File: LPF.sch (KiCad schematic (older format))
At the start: 142 parts, among them J1 Conn_02x05_Counter_Clockwise, P1 SMA, P2 SMA, P3 SMA, P4 SMA, P5 SMA, P6 SMA

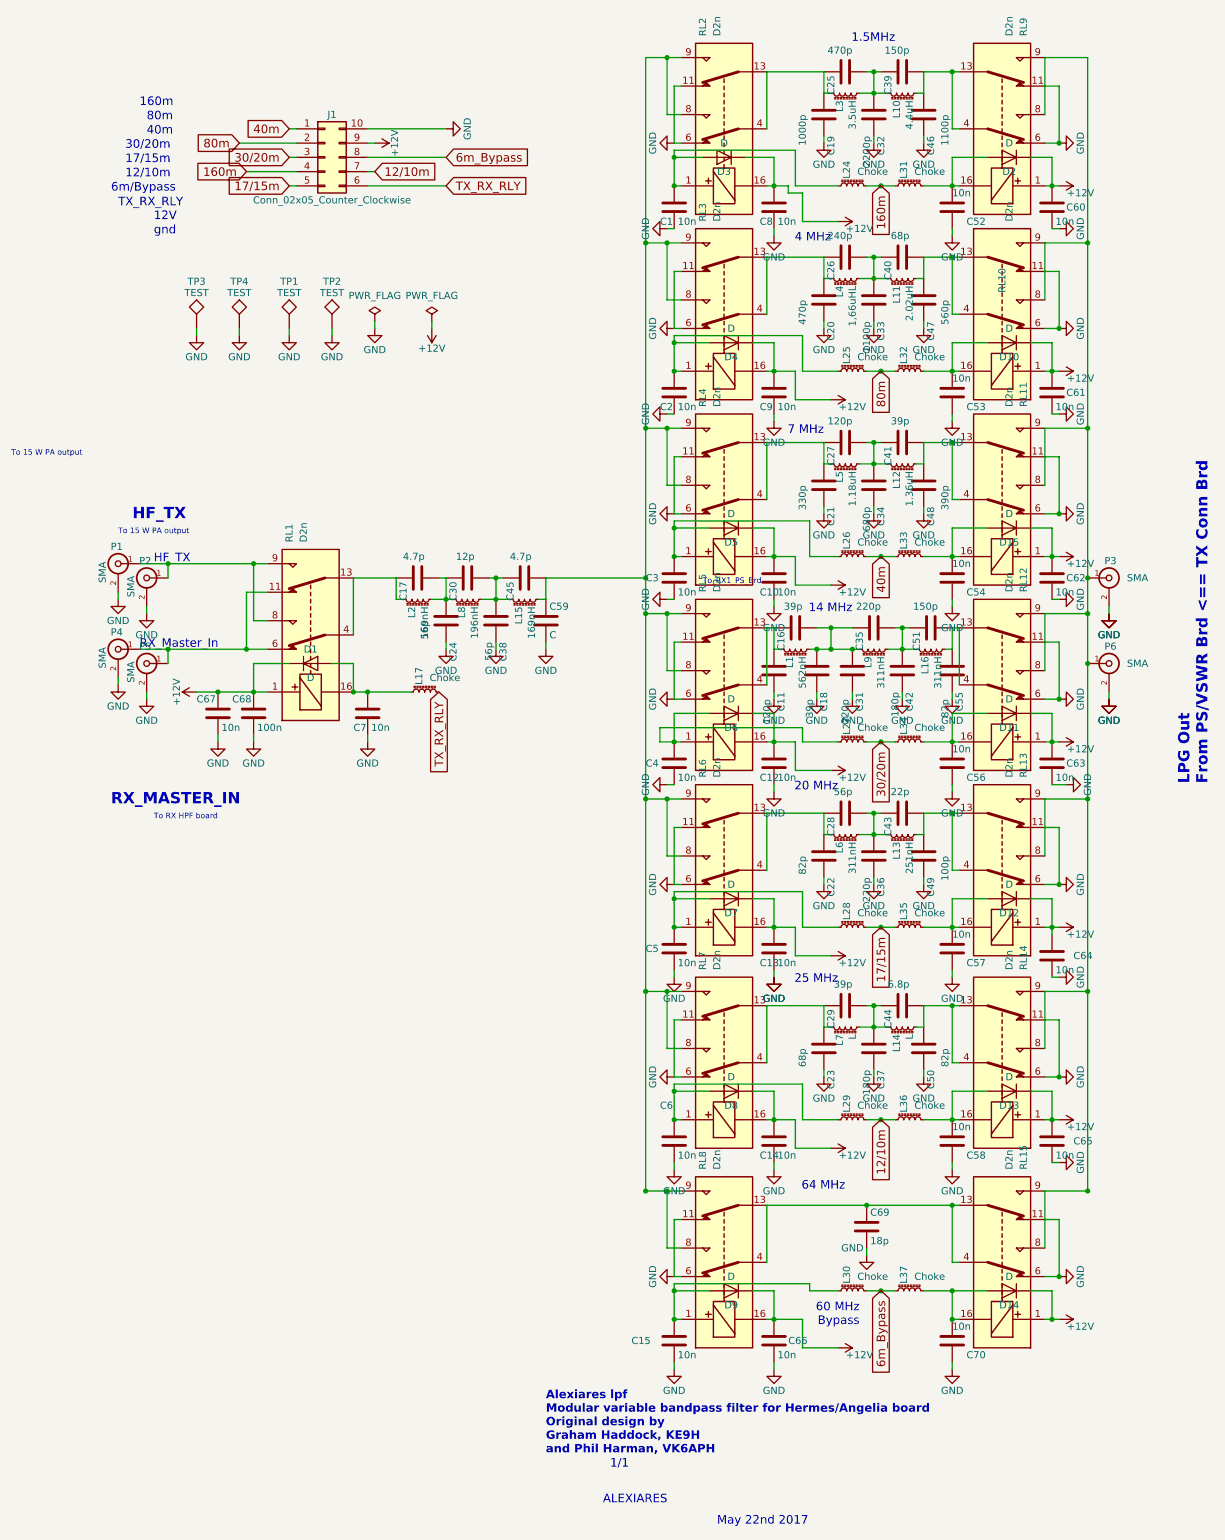
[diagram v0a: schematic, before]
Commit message: inductance value modified
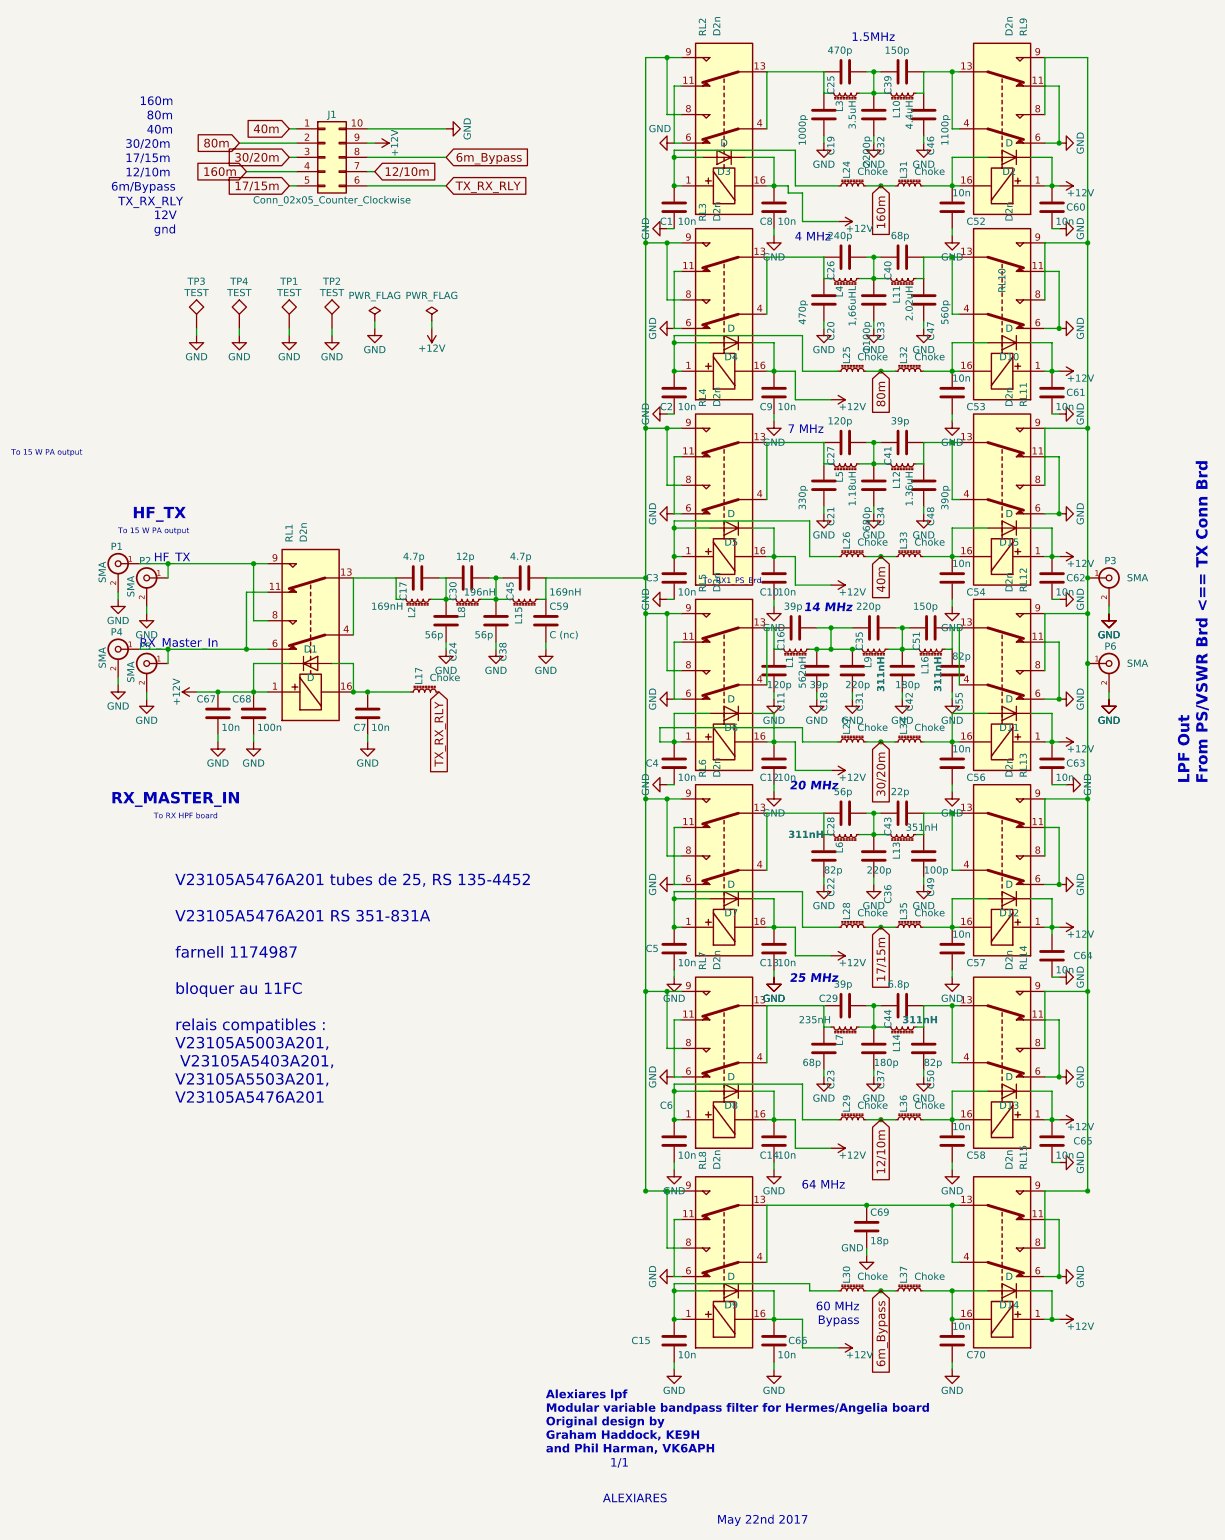
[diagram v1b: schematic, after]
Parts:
- C59: value C -> C (nc)
- L13: value 251nH -> 351nH
- L14: value L -> 311nH
- L7: value L -> 235nH
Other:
- note added: "LPF Out\nFrom PS/VSWR Brd <== TX Conn Brd"
- note added: "V23105A5476A201 tubes de 25, RS 135-4452\n\nV23105A5476A201 RS 351-831A\n\nfarnell 1174987 \n\nbloquer au 11FC\n\nrelais compatibles : \nV23105A5003A201,\n V23105A5403A201, \nV23105A5503A201, \nV23105A5476A201"
- note removed: "LPG Out\nFrom PS/VSWR Brd <== TX Conn Brd"
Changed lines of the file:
@@
 EESchema Schematic File Version 2
-LIBS:power
-LIBS:device
-LIBS:transistors
-LIBS:conn
-LIBS:linear
-LIBS:regul
-LIBS:7805d-pack
 LIBS:d2n
+LIBS:Connector_Generic
+LIBS:Device
+LIBS:power
 LIBS:LPF-cache
 EELAYER 25 0
@@
 Text Notes 4700 4450 0    39   ~ 0
 To_RX1_PS_Brd \n
-Text Notes 5650 7250 2    60   ~ 0
+Text Notes 5650 7250 2    60   Italic 12
 25 MHz\n
 $Comp
@@
 P 4500 1350
 F 0 "#PWR03" H 4500 1100 50  0001 C CNN
-F 1 "GND" H 4500 1200 50  0000 C CNN
+F 1 "GND" V 4400 1250 50  0000 C CNN
 F 2 "" H 4500 1350 50  0000 C CNN
 F 3 "" H 4500 1350 50  0000 C CNN
@@
 P 6300 4900
 F 0 "L16" H 6350 4940 50  0000 L CNN
-F 1 "311nH" H 6350 4850 50  0000 L CNN
+F 1 "311nH" H 6350 4850 50  0000 L CNB
 F 2 "T50:T50_V_THT" H 6300 4900 50  0001 C CNN
 F 3 "" H 6300 4900 50  0000 C CNN
@@
 P 6450 5050
 F 0 "C55" V 6500 5200 50  0000 L CNN
-F 1 "82p" V 6400 5250 50  0000 L CNN
+F 1 "82p" H 6450 4950 50  0000 L CNN
 F 2 "ATC_B:ATC_500_HandSoldering" H 6488 4900 50  0001 C CNN
 F 3 "" H 6450 5050 50  0001 C CNN
@@
 P 6100 5050
 F 0 "C42" V 6150 5200 50  0000 L CNN
-F 1 "180p" V 6050 5200 50  0000 L CNN
+F 1 "180p" H 6050 5150 50  0000 L CNN
 F 2 "ATC_B:ATC_500_HandSoldering" H 6138 4900 50  0001 C CNN
 F 3 "" H 6100 5050 50  0001 C CNN
@@
 P 5900 4900
 F 0 "L9" H 5950 4940 50  0000 L CNN
-F 1 "311nH" H 5950 4850 50  0000 L CNN
+F 1 "311nH" H 5950 4850 50  0000 L CNB
 F 2 "T50:T50_V_THT" H 5900 4900 50  0001 C CNN
 F 3 "" H 5900 4900 50  0000 C CNN
@@
 P 5750 5050
 F 0 "C31" V 5800 5200 50  0000 L CNN
-F 1 "220p" V 5700 5250 50  0000 L CNN
+F 1 "220p" H 5700 5150 50  0000 L CNN
 F 2 "ATC_B:ATC_500_HandSoldering" H 5788 4900 50  0001 C CNN
 F 3 "" H 5750 5050 50  0001 C CNN
@@
 P 3450 4550
 F 0 "L15" H 3500 4590 50  0000 L CNN
-F 1 "169nH" H 3500 4500 50  0000 L CNN
+F 1 "169nH" V 3400 4150 50  0000 L CNN
 F 2 "T50:T50_V_THT" H 3450 4550 50  0001 C CNN
 F 3 "" H 3450 4550 50  0000 C CNN
@@
 P 3250 4700
 F 0 "C38" V 3300 4850 50  0000 L CNN
-F 1 "56p" V 3200 4850 50  0000 L CNN
+F 1 "56p" H 3100 4800 50  0000 L CNN
 F 2 "ATC_B:ATC_500_HandSoldering" H 3288 4550 50  0001 C CNN
 F 3 "" H 3250 4700 50  0001 C CNN
@@
 P 3050 4550
 F 0 "L8" H 3100 4590 50  0000 L CNN
-F 1 "196nH" H 3100 4500 50  0000 L CNN
+F 1 "196nH" V 3000 4350 50  0000 L CNN
 F 2 "T50:T50_V_THT" H 3050 4550 50  0001 C CNN
 F 3 "" H 3050 4550 50  0000 C CNN
@@
 P 2900 4700
 F 0 "C24" V 2950 4850 50  0000 L CNN
-F 1 "56p" V 2750 4700 50  0000 L CNN
+F 1 "56p" H 2750 4800 50  0000 L CNN
 F 2 "ATC_B:ATC_500_HandSoldering" H 2938 4550 50  0001 C CNN
 F 3 "" H 2900 4700 50  0001 C CNN
@@
 P 6100 6200
 F 0 "L13" H 6150 6240 50  0000 L CNN
-F 1 "251nH" H 6150 6150 50  0000 L CNN
+F 1 "351nH" V 6050 5950 50  0000 L CNN
 F 2 "T50:T50_V_THT" H 6100 6200 50  0001 C CNN
 F 3 "" H 6100 6200 50  0000 C CNN
@@
 P 6250 6350
 F 0 "C49" V 6300 6500 50  0000 L CNN
-F 1 "100p" V 6400 6350 50  0000 L CNN
+F 1 "100p" H 6250 6450 50  0000 L CNN
 F 2 "ATC_B:ATC_500_HandSoldering" H 6288 6200 50  0001 C CNN
 F 3 "" H 6250 6350 50  0001 C CNN
@@
 U 1 1 592DB32A
 P 5900 6350
-F 0 "C36" V 5950 6500 50  0000 L CNN
-F 1 "220p" V 5850 6500 50  0000 L CNN
+F 0 "C36" V 6000 6550 50  0000 L CNN
+F 1 "220p" H 5850 6450 50  0000 L CNN
 F 2 "ATC_B:ATC_500_HandSoldering" H 5938 6200 50  0001 C CNN
 F 3 "" H 5900 6350 50  0001 C CNN
@@
 P 5700 6200
 F 0 "L6" H 5750 6240 50  0000 L CNN
-F 1 "311nH" H 5750 6150 50  0000 L CNN
+F 1 "311nH" V 5700 6350 50  0000 L CNB
 F 2 "T50:T50_V_THT" H 5700 6200 50  0001 C CNN
 F 3 "" H 5700 6200 50  0000 C CNN
@@
 P 5550 6350
 F 0 "C22" V 5600 6500 50  0000 L CNN
-F 1 "82p" V 5400 6350 50  0000 L CNN
+F 1 "82p" H 5550 6450 50  0000 L CNN
 F 2 "ATC_B:ATC_500_HandSoldering" H 5588 6200 50  0001 C CNN
 F 3 "" H 5550 6350 50  0001 C CNN
@@
 P 6100 7550
 F 0 "L14" H 6150 7590 50  0000 L CNN
-F 1 "L" H 6150 7500 50  0000 L CNN
+F 1 "311nH" V 6050 7300 50  0000 L CNB
 F 2 "T50:T50_V_THT" H 6100 7550 50  0001 C CNN
 F 3 "" H 6100 7550 50  0000 C CNN
@@
 P 6250 7700
 F 0 "C50" V 6300 7850 50  0000 L CNN
-F 1 "82p" V 6400 7700 50  0000 L CNN
+F 1 "82p" H 6250 7800 50  0000 L CNN
 F 2 "ATC_B:ATC_500_HandSoldering" H 6288 7550 50  0001 C CNN
 F 3 "" H 6250 7700 50  0001 C CNN
@@
 P 5900 7700
 F 0 "C37" V 5950 7850 50  0000 L CNN
-F 1 "180p" V 5850 7850 50  0000 L CNN
+F 1 "180p" H 5900 7800 50  0000 L CNN
 F 2 "ATC_B:ATC_500_HandSoldering" H 5938 7550 50  0001 C CNN
 F 3 "" H 5900 7700 50  0001 C CNN
@@
 U 1 1 592DB33F
 P 5700 7400
-F 0 "C29" H 5725 7500 50  0000 L CNN
+F 0 "C29" V 5650 7450 50  0000 L CNN
 F 1 "39p" V 5550 7350 50  0000 L CNN
 F 2 "ATC_B:ATC_500_HandSoldering" H 5738 7250 50  0001 C CNN
@@
 P 5700 7550
 F 0 "L7" H 5750 7590 50  0000 L CNN
-F 1 "L" H 5750 7500 50  0000 L CNN
+F 1 "235nH" V 5650 7650 50  0000 L CNN
 F 2 "T50:T50_V_THT" H 5700 7550 50  0001 C CNN
 F 3 "" H 5700 7550 50  0000 C CNN
@@
 P 5550 7700
 F 0 "C23" V 5600 7850 50  0000 L CNN
-F 1 "68p" V 5400 7700 50  0000 L CNN
+F 1 "68p" H 5400 7800 50  0000 L CNN
 F 2 "ATC_B:ATC_500_HandSoldering" H 5588 7550 50  0001 C CNN
 F 3 "" H 5550 7700 50  0001 C CNN
@@
 P 2700 4550
 F 0 "L2" H 2750 4590 50  0000 L CNN
-F 1 "169nH" H 2750 4500 50  0000 L CNN
+F 1 "169nH" V 2750 4650 50  0000 L CNN
 F 2 "T50:T50_V_THT" H 2700 4550 50  0001 C CNN
 F 3 "" H 2700 4550 50  0000 C CNN
@@
 P 5200 5050
 F 0 "C11" V 5250 5200 50  0000 L CNN
-F 1 "120p" V 5150 5250 50  0000 L CNN
+F 1 "120p" H 5150 5150 50  0000 L CNN
 F 2 "ATC_B:ATC_500_HandSoldering" H 5238 4900 50  0001 C CNN
 F 3 "" H 5200 5050 50  0001 C CNN
@@
 P 5500 5050
 F 0 "C18" V 5550 5200 50  0000 L CNN
-F 1 "39p" V 5450 5250 50  0000 L CNN
+F 1 "39p" H 5450 5150 50  0000 L CNN
 F 2 "ATC_B:ATC_500_HandSoldering" H 5538 4900 50  0001 C CNN
 F 3 "" H 5500 5050 50  0001 C CNN
@@
 	1    0    0    -1
 $EndComp
-Text Notes 5650 5900 2    60   ~ 0
+Text Notes 5650 5900 2    60   Italic 12
 20 MHz\n
 Text Notes 5550 3400 2    60   ~ 0
@@
 Text Notes 6050 650  2    60   ~ 0
 1.5MHz
-Text Notes 5750 4650 2    60   ~ 0
+Text Notes 5750 4650 2    60   Italic 12
 14 MHz
 Text Notes 5700 8700 2    60   ~ 0
@@
 To 15 W PA output\n
 Text Notes 8250 5850 1    79   ~ 16
-LPG Out\nFrom PS/VSWR Brd <== TX Conn Brd
+LPF Out\nFrom PS/VSWR Brd <== TX Conn Brd
 $Comp
 L +12V #PWR075
@@
 P 3600 4700
 F 0 "C59" H 3625 4800 50  0000 L CNN
-F 1 "C" H 3625 4600 50  0000 L CNN
+F 1 "C (nc)" H 3625 4600 50  0000 L CNN
 F 2 "ATC_B:ATC_500_HandSoldering" H 3638 4550 50  0001 C CNN
 F 3 "" H 3600 4700 50  0001 C CNN
@@
 	7550 5200 7550 5250
 Connection ~ 7400 5000
+Text Notes 1000 8100 0    79   ~ 0
+V23105A5476A201 tubes de 25, RS 135-4452\n\nV23105A5476A201 RS 351-831A\n\nfarnell 1174987 \n\nbloquer au 11FC\n\nrelais compatibles : \nV23105A5003A201,\n V23105A5403A201, \nV23105A5503A201, \nV23105A5476A201
 $EndSCHEMATC

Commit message: minor silk changes
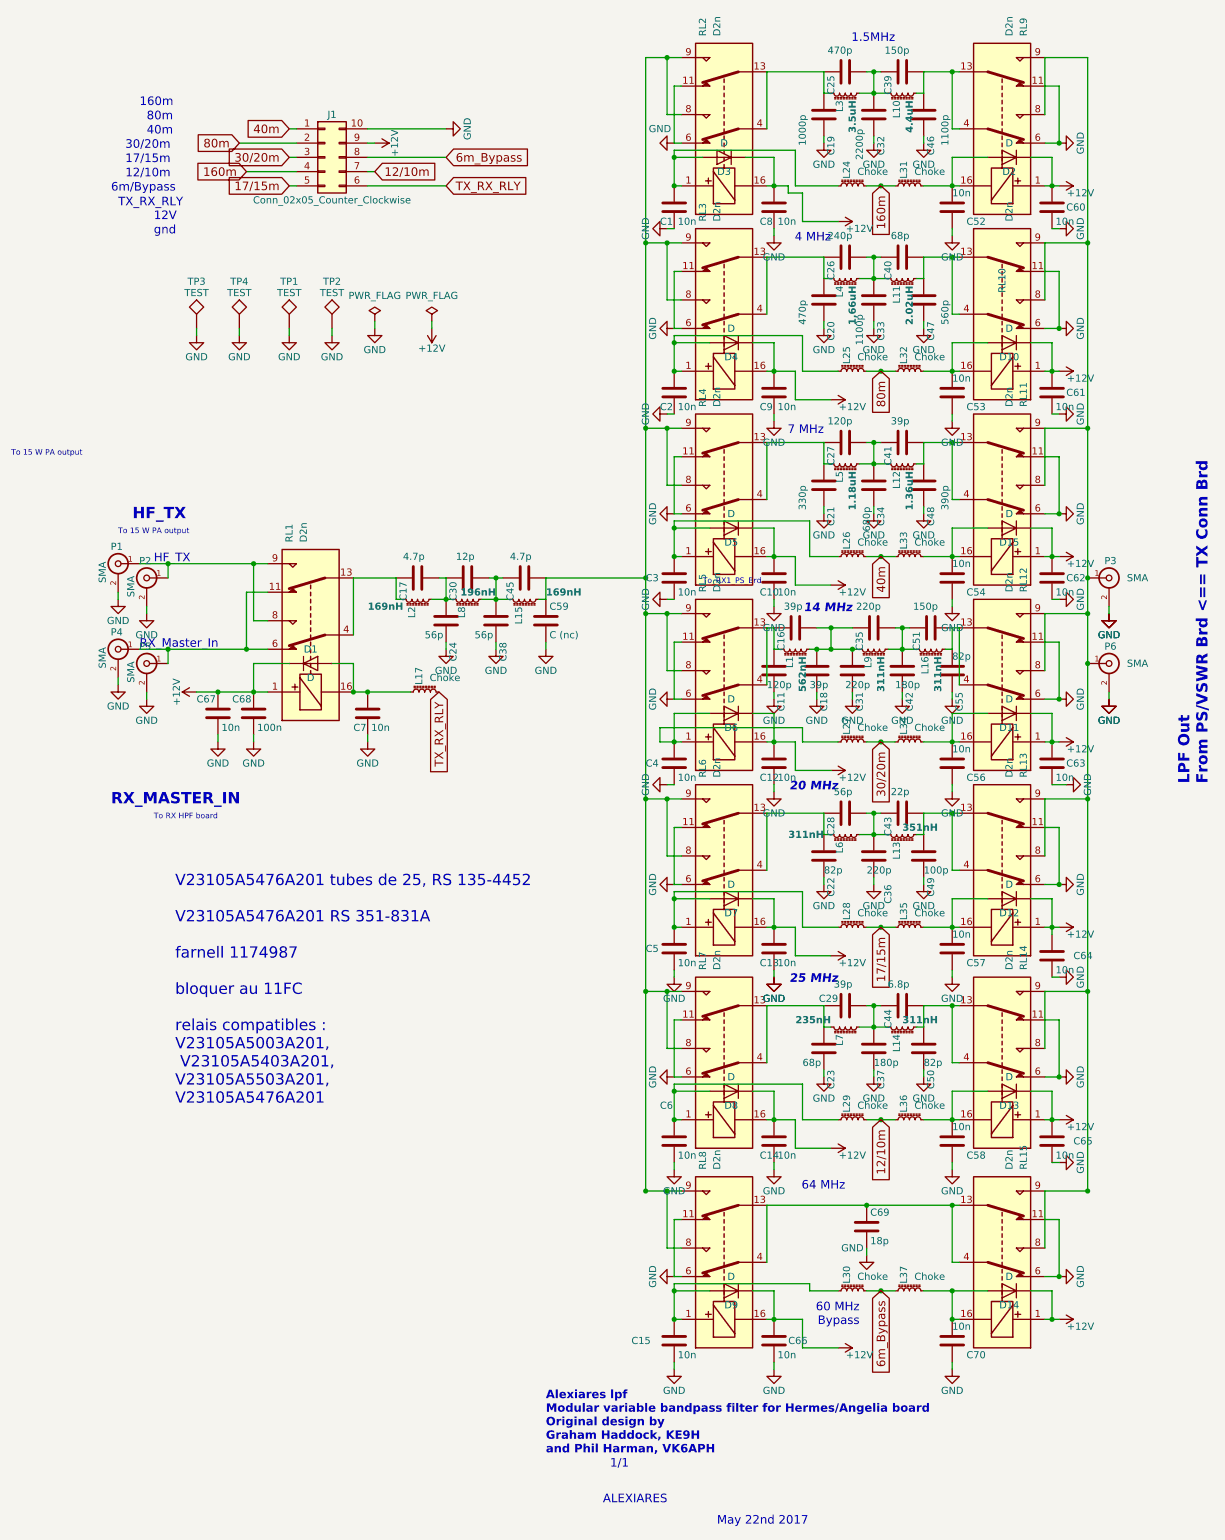
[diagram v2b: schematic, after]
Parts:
- L4: value 1,66uHL -> 1,66uH
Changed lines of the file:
@@
 P 6100 1000
 F 0 "L10" H 6150 1040 50  0000 L CNN
-F 1 "4.4uH" H 6150 950 50  0000 L CNN
+F 1 "4.4uH" H 6150 950 50  0000 L CNB
 F 2 "T50:T50_V_THT" H 6100 1000 50  0001 C CNN
 F 3 "" H 6100 1000 50  0000 C CNN
@@
 P 5900 1150
 F 0 "C32" V 5950 1300 50  0000 L CNN
-F 1 "2200p" V 5850 1300 50  0000 L CNN
+F 1 "2200p" V 5800 1250 50  0000 L CNN
 F 2 "ATC_B:ATC_500_HandSoldering" H 5938 1000 50  0001 C CNN
 F 3 "" H 5900 1150 50  0001 C CNN
@@
 P 5700 1000
 F 0 "L3" H 5750 1040 50  0000 L CNN
-F 1 "3.5uH" H 5750 950 50  0000 L CNN
+F 1 "3.5uH" H 5750 950 50  0000 L CNB
 F 2 "T50:T50_V_THT" H 5700 1000 50  0001 C CNN
 F 3 "" H 5700 1000 50  0000 C CNN
@@
 P 6100 2300
 F 0 "L11" H 6150 2340 50  0000 L CNN
-F 1 "2.02uH" H 6150 2250 50  0000 L CNN
+F 1 "2.02uH" H 6150 2250 50  0000 L CNB
 F 2 "T50:T50_V_THT" H 6100 2300 50  0001 C CNN
 F 3 "" H 6100 2300 50  0000 C CNN
@@
 P 5900 2450
 F 0 "C33" V 5950 2600 50  0000 L CNN
-F 1 "1100p" V 5850 2600 50  0000 L CNN
+F 1 "1100p" V 5800 2550 50  0000 L CNN
 F 2 "ATC_B:ATC_500_HandSoldering" H 5938 2300 50  0001 C CNN
 F 3 "" H 5900 2450 50  0001 C CNN
@@
 P 5700 2300
 F 0 "L4" H 5750 2340 50  0000 L CNN
-F 1 "1,66uHL" H 5750 2250 50  0000 L CNN
+F 1 "1,66uH" H 5750 2250 50  0000 L CNB
 F 2 "T50:T50_V_THT" H 5700 2300 50  0001 C CNN
 F 3 "" H 5700 2300 50  0000 C CNN
@@
 P 6100 3600
 F 0 "L12" H 6150 3640 50  0000 L CNN
-F 1 "1.36uH" H 6150 3550 50  0000 L CNN
+F 1 "1.36uH" H 6150 3550 50  0000 L CNB
 F 2 "T50:T50_V_THT" H 6100 3600 50  0001 C CNN
 F 3 "" H 6100 3600 50  0000 C CNN
@@
 P 5700 3600
 F 0 "L5" H 5750 3640 50  0000 L CNN
-F 1 "1.18uH" H 5750 3550 50  0000 L CNN
+F 1 "1.18uH" H 5750 3550 50  0000 L CNB
 F 2 "T50:T50_V_THT" H 5700 3600 50  0001 C CNN
 F 3 "" H 5700 3600 50  0000 C CNN
@@
 P 3450 4550
 F 0 "L15" H 3500 4590 50  0000 L CNN
-F 1 "169nH" V 3400 4150 50  0000 L CNN
+F 1 "169nH" V 3400 4150 50  0000 L CNB
 F 2 "T50:T50_V_THT" H 3450 4550 50  0001 C CNN
 F 3 "" H 3450 4550 50  0000 C CNN
@@
 P 3050 4550
 F 0 "L8" H 3100 4590 50  0000 L CNN
-F 1 "196nH" V 3000 4350 50  0000 L CNN
+F 1 "196nH" V 3000 4350 50  0000 L CNB
 F 2 "T50:T50_V_THT" H 3050 4550 50  0001 C CNN
 F 3 "" H 3050 4550 50  0000 C CNN
@@
 P 6100 6200
 F 0 "L13" H 6150 6240 50  0000 L CNN
-F 1 "351nH" V 6050 5950 50  0000 L CNN
+F 1 "351nH" V 6050 5950 50  0000 L CNB
 F 2 "T50:T50_V_THT" H 6100 6200 50  0001 C CNN
 F 3 "" H 6100 6200 50  0000 C CNN
@@
 P 5700 7550
 F 0 "L7" H 5750 7590 50  0000 L CNN
-F 1 "235nH" V 5650 7650 50  0000 L CNN
+F 1 "235nH" V 5650 7650 50  0000 L CNB
 F 2 "T50:T50_V_THT" H 5700 7550 50  0001 C CNN
 F 3 "" H 5700 7550 50  0000 C CNN
@@
 P 2700 4550
 F 0 "L2" H 2750 4590 50  0000 L CNN
-F 1 "169nH" V 2750 4650 50  0000 L CNN
+F 1 "169nH" V 2750 4650 50  0000 L CNB
 F 2 "T50:T50_V_THT" H 2700 4550 50  0001 C CNN
 F 3 "" H 2700 4550 50  0000 C CNN
@@
 P 5350 4900
 F 0 "L1" H 5400 4940 50  0000 L CNN
-F 1 "562nH" H 5400 4850 50  0000 L CNN
+F 1 "562nH" H 5400 4850 50  0000 L CNB
 F 2 "T50:T50_V_THT" H 5350 4900 50  0001 C CNN
 F 3 "" H 5350 4900 50  0000 C CNN
